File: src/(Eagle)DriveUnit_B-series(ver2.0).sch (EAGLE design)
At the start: 55 parts, among them IC1 A3921, SW1 TVAF06-A020B-R, SW2 TVAF06-A020B-R, SW3 THAF01-NC-R, SW4 SS-12D00G3

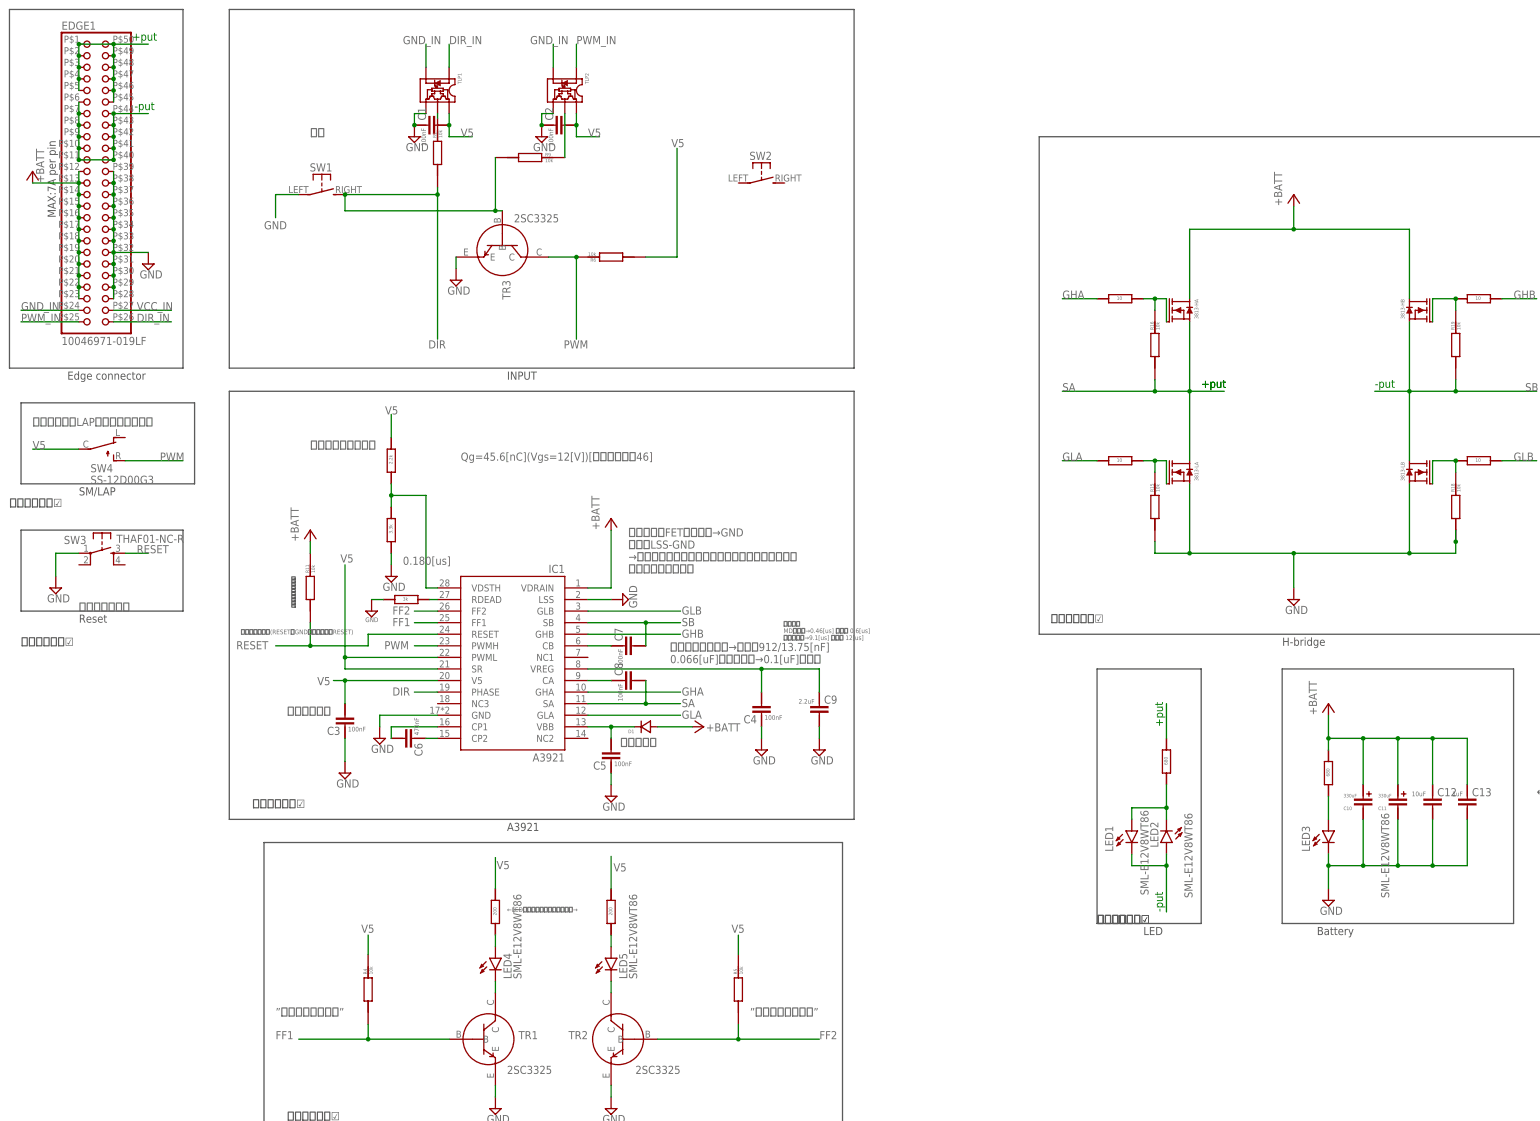
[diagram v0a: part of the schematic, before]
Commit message: 入力部分の追加
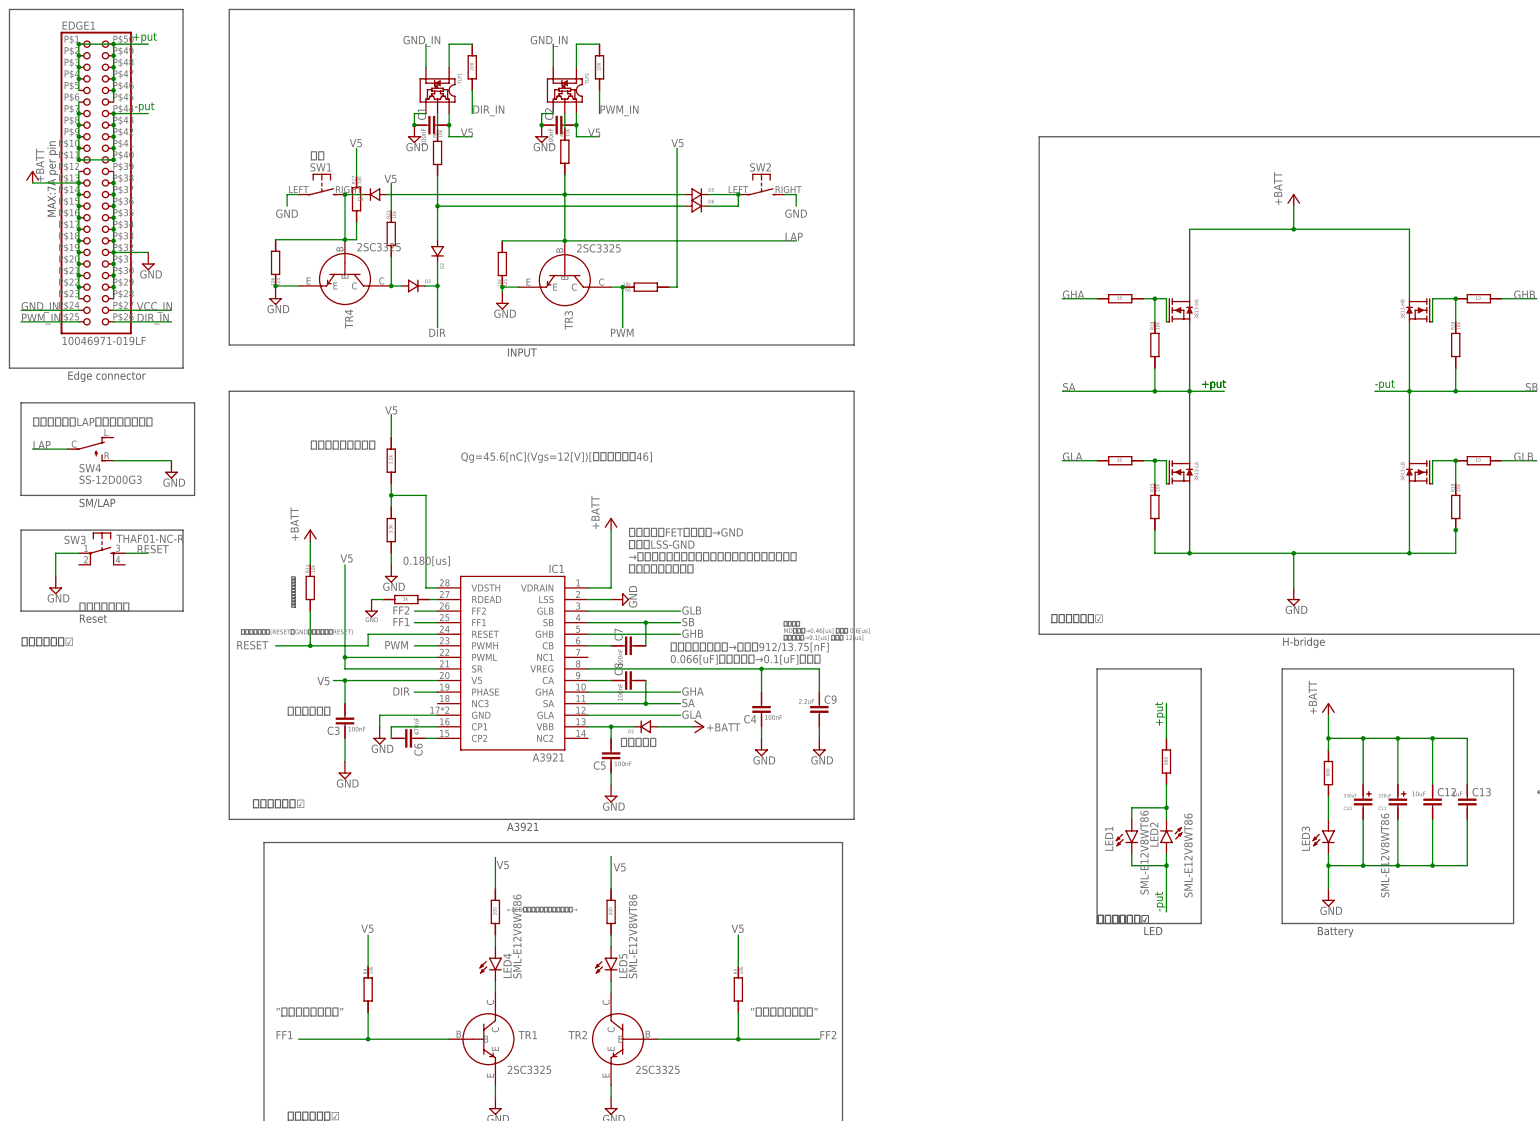
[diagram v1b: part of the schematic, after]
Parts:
- added D2, D3, D4, D5, D6: GS1010FL, GS1010FL:GS1010FL
- added R17, R23, R24, R25: RG2012, RG2012:RG2012
- added R26, R27: RG2012N-201-W-T1, RG2012N-201-W-T1:RG2012N-201-W-T1
- added TR4: 2SC3325, 2SC3325:2SC3325
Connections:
- new net LAP: D4.A, D5.A, R25.LEFT, R9.LEFT, SW4.C, TR3.B
- new net N$12: D3.A, R23.LEFT, TR4.C
- new net N$17: D4.C, R17.LEFT, R24.LEFT, SW1.S, TR4.B
- new net N$20: D5.C, D6.C, SW2.P
- new net N$23: R26.P$1, TLP1.ANODE
- new net N$24: R27.P$1, TLP2.ANODE
- net DIR: now also D2.A, D2.C, D3.C, D6.A; no longer R9.LEFT, SW1.S, TR3.B
- net DIR_IN: now also R26.P$2; no longer TLP1.ANODE
- net GND: now also R24.RIGHT, R25.RIGHT, SW2.S, SW4.R, TR4.E
- net PWM: no longer SW4.R
- net PWM_IN: now also R27.P$2; no longer TLP2.ANODE
- net V5: now also R17.RIGHT, R23.RIGHT; no longer SW4.C
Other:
- moved on the sheet: R6, R9, SW2, SW4, TR3

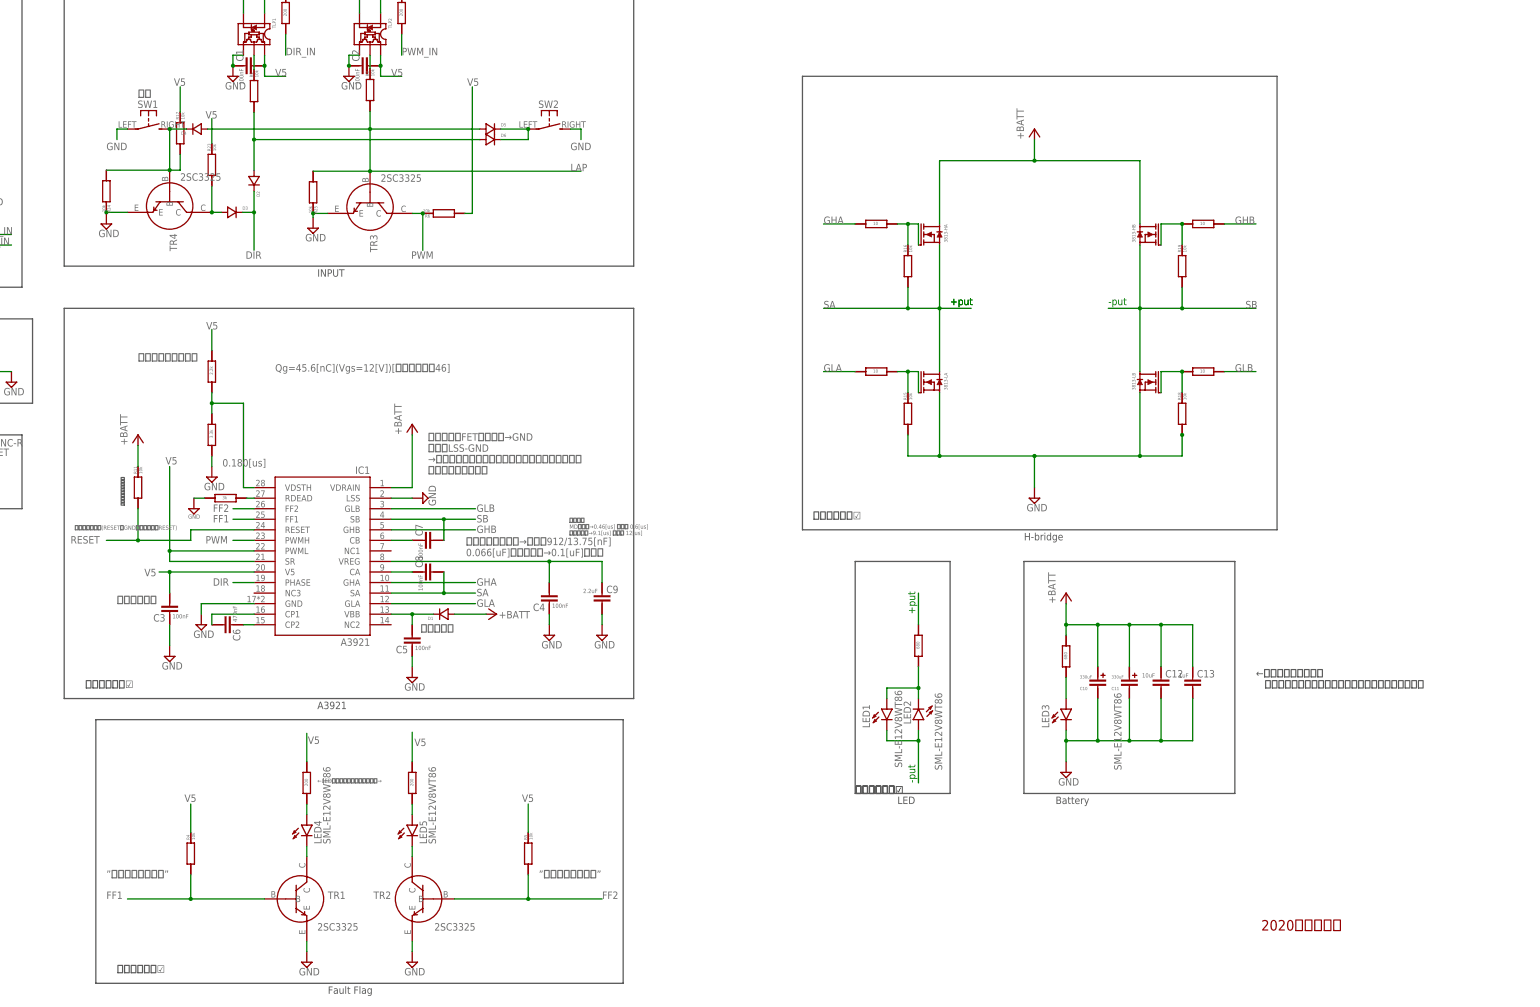
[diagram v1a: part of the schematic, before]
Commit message: 回路図の偏向
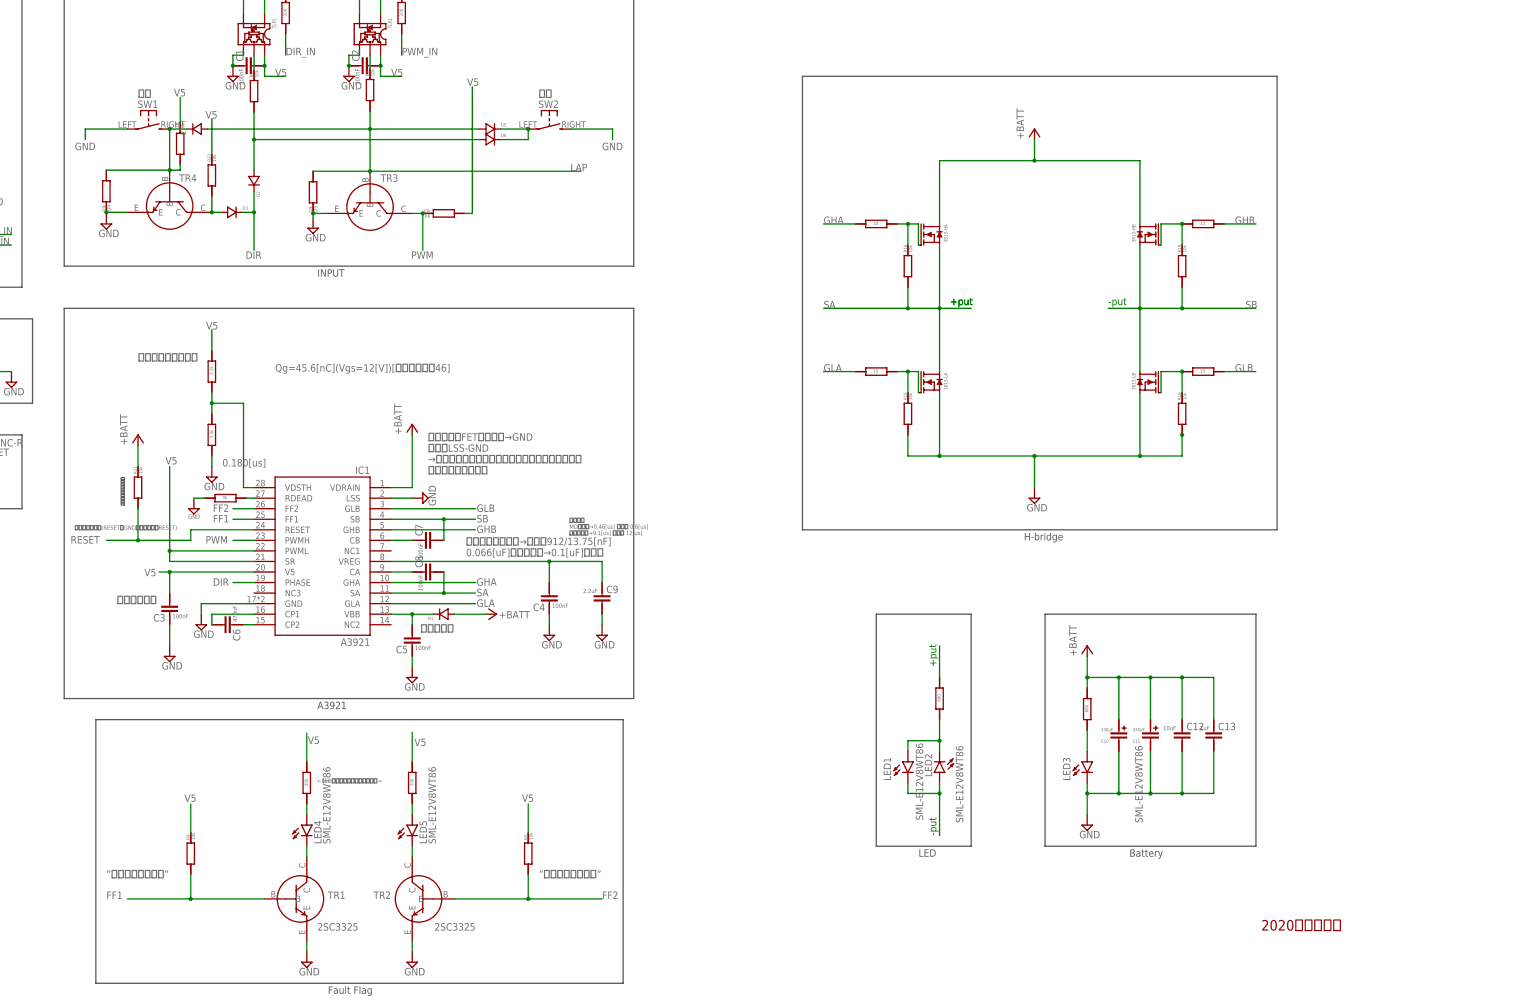
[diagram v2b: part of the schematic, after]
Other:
- note added: "逆転"
- note removed: "←大型電解コンデンサ スイッチング時間により容量が変わるので最後にする"
- moved on the sheet: C10, C11, C12, C13, LED1, LED2, LED3, R17, R23

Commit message: [fix]デッドタイムを100kΩ可変抵抗で調整できるように変更
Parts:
- added R28: 100k, GF063P B104K:GF063PB104K
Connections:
- new net N$16: R13.P$2, R28.RIGHT
- net GND: now also R28.LEFT; no longer R13.P$2
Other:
- note removed: "Qg=45.6[nC](Vgs=12[V])[有効数字考慮46]"
- note removed: "”オープンドレイン”"
- note removed: "←LEDが壊れないくらいの抵抗値→"
- note removed: "リセットボタン"
- note removed: "別に適当でよさそう"
- note removed: "短絡させるとLAP方式になるよ！！"
- note removed: "部品選定完了☑"

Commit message: [add]電流センサ周りの配線_1
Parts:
- added IC2: CZ3A07, CZ3A07:CZ3A07
- added JP1: (no value), con-jst-xh:03-JST
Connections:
- new net VOUT: JP1.2
- net GND_IN: now also IC2.OCD2, IC2.REF2, IC2.VSS1, JP1.1
- net SA: now also IC2.IP
- net SB: now also IC2.IN
- net VCC_IN: now also JP1.3
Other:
- note added: "80Aの場合 1.29314286[V]"
- note added: "VREF1 [mV] = 2500 - |IOCDTH1|[A] × (528/35)"
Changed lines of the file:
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@@
 <part name="SUPPLY21" library="supply2" library_urn="urn:adsk.eagle:library:372" deviceset="GND" device=""/>
 <part name="R28" library="GF063P B104K" deviceset="GF063PB104K" device="" value="100k"/>
+<part name="FRAME2" library="frames" library_urn="urn:adsk.eagle:library:229" deviceset="A5L-LOC" device=""/>
+<part name="IC2" library="CZ3A07" deviceset="CZ3A07" device=""/>
+<part name="JP1" library="con-jst-xh" deviceset="03-JST" device=""/>
 </parts>
 <sheets>
@@
 <sheet>
 <plain>
+<text x="140.97" y="20.32" size="2.54" layer="94">2020年度回路班</text>
+<text x="48.26" y="79.502" size="1.778" layer="91">+put</text>
+<text x="48.26" y="69.342" size="1.778" layer="91">-put</text>
+<text x="50.8" y="96.52" size="1.27" layer="97">VREF1 [mV] = 2500 - |IOCDTH1|[A] × (528/35)</text>
+<text x="63.5" y="91.44" size="1.27" layer="97">80Aの場合
+1.29314286[V]</text>
 </plain>
 <instances>
+<instance part="FRAME2" gate="G$1" x="0" y="0" smashed="yes">
+<attribute name="DRAWING_NAME" x="140.97" y="15.24" size="2.54" layer="94"/>
+<attribute name="LAST_DATE_TIME" x="140.97" y="10.16" size="2.286" layer="94"/>
+<attribute name="SHEET" x="154.305" y="5.08" size="2.54" layer="94"/>
+</instance>
+<instance part="IC2" gate="G$1" x="66.294" y="74.93" smashed="yes">
+<attribute name="NAME" x="59.944" y="85.725" size="1.778" layer="95"/>
+<attribute name="VALUE" x="59.944" y="59.69" size="1.778" layer="96"/>
+</instance>
+<instance part="JP1" gate="G$1" x="134.62" y="73.66" smashed="yes">
+<attribute name="VALUE" x="133.35" y="66.04" size="1.778" layer="96"/>
+<attribute name="NAME" x="133.35" y="79.502" size="1.778" layer="95"/>
+</instance>
 </instances>
 <busses>
 </busses>
 <nets>
+<net name="SA" class="0">
+<segment>
+<pinref part="IC2" gate="G$1" pin="IP"/>
+<wire x1="63.754" y1="78.74" x2="48.26" y2="78.74" width="0.1524" layer="91"/>
+</segment>
+</net>
+<net name="SB" class="0">
+<segment>
+<pinref part="IC2" gate="G$1" pin="IN"/>
+<wire x1="63.754" y1="68.58" x2="48.26" y2="68.58" width="0.1524" layer="91"/>
+</segment>
+</net>
+<net name="GND_IN" class="0">
+<segment>
+<pinref part="JP1" gate="G$1" pin="1"/>
+<wire x1="142.24" y1="71.12" x2="147.32" y2="71.12" width="0.1524" layer="91"/>
+<wire x1="147.32" y1="71.12" x2="147.32" y2="66.04" width="0.1524" layer="91"/>
+<label x="142.24" y="63.5" size="2.54" layer="95"/>
+</segment>
+<segment>
+<pinref part="IC2" gate="G$1" pin="VSS1"/>
+<wire x1="71.374" y1="64.77" x2="93.98" y2="64.77" width="0.1524" layer="91"/>
+<wire x1="93.98" y1="64.77" x2="93.98" y2="53.34" width="0.1524" layer="91"/>
+<label x="93.98" y="53.34" size="2.54" layer="95"/>
+<pinref part="IC2" gate="G$1" pin="REF2"/>
+<wire x1="71.374" y1="80.01" x2="93.98" y2="80.01" width="0.1524" layer="91"/>
+<wire x1="93.98" y1="80.01" x2="93.98" y2="69.85" width="0.1524" layer="91"/>
+<junction x="93.98" y="64.77"/>
+<pinref part="IC2" gate="G$1" pin="OCD2"/>
+<wire x1="93.98" y1="69.85" x2="93.98" y2="64.77" width="0.1524" layer="91"/>
+<wire x1="71.374" y1="69.85" x2="93.98" y2="69.85" width="0.1524" layer="91"/>
+<junction x="93.98" y="69.85"/>
+</segment>
+</net>
+<net name="VCC_IN" class="0">
+<segment>
+<pinref part="JP1" gate="G$1" pin="3"/>
+<wire x1="142.24" y1="76.2" x2="147.32" y2="76.2" width="0.1524" layer="91"/>
+<wire x1="147.32" y1="76.2" x2="147.32" y2="83.82" width="0.1524" layer="91"/>
+<label x="142.24" y="83.82" size="2.54" layer="95"/>
+</segment>
+</net>
+<net name="VOUT" class="0">
+<segment>
+<pinref part="JP1" gate="G$1" pin="2"/>
+<wire x1="142.24" y1="73.66" x2="157.48" y2="73.66" width="0.1524" layer="91"/>
+<label x="149.86" y="73.66" size="2.54" layer="95"/>
+</segment>
+</net>
 </nets>
 </sheet>
